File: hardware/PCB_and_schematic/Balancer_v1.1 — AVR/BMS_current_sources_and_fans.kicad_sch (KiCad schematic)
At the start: 90 parts, among them J11 HEATSING_TEMP1, J3 Conn_01x03, J4 HEATSING_TEMP1, J5 FAN1, J6 FAN2, J7 BATT_12V, Q10 TIP41C, Q11 TIP41C, Q12 BC817, Q13 BD238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

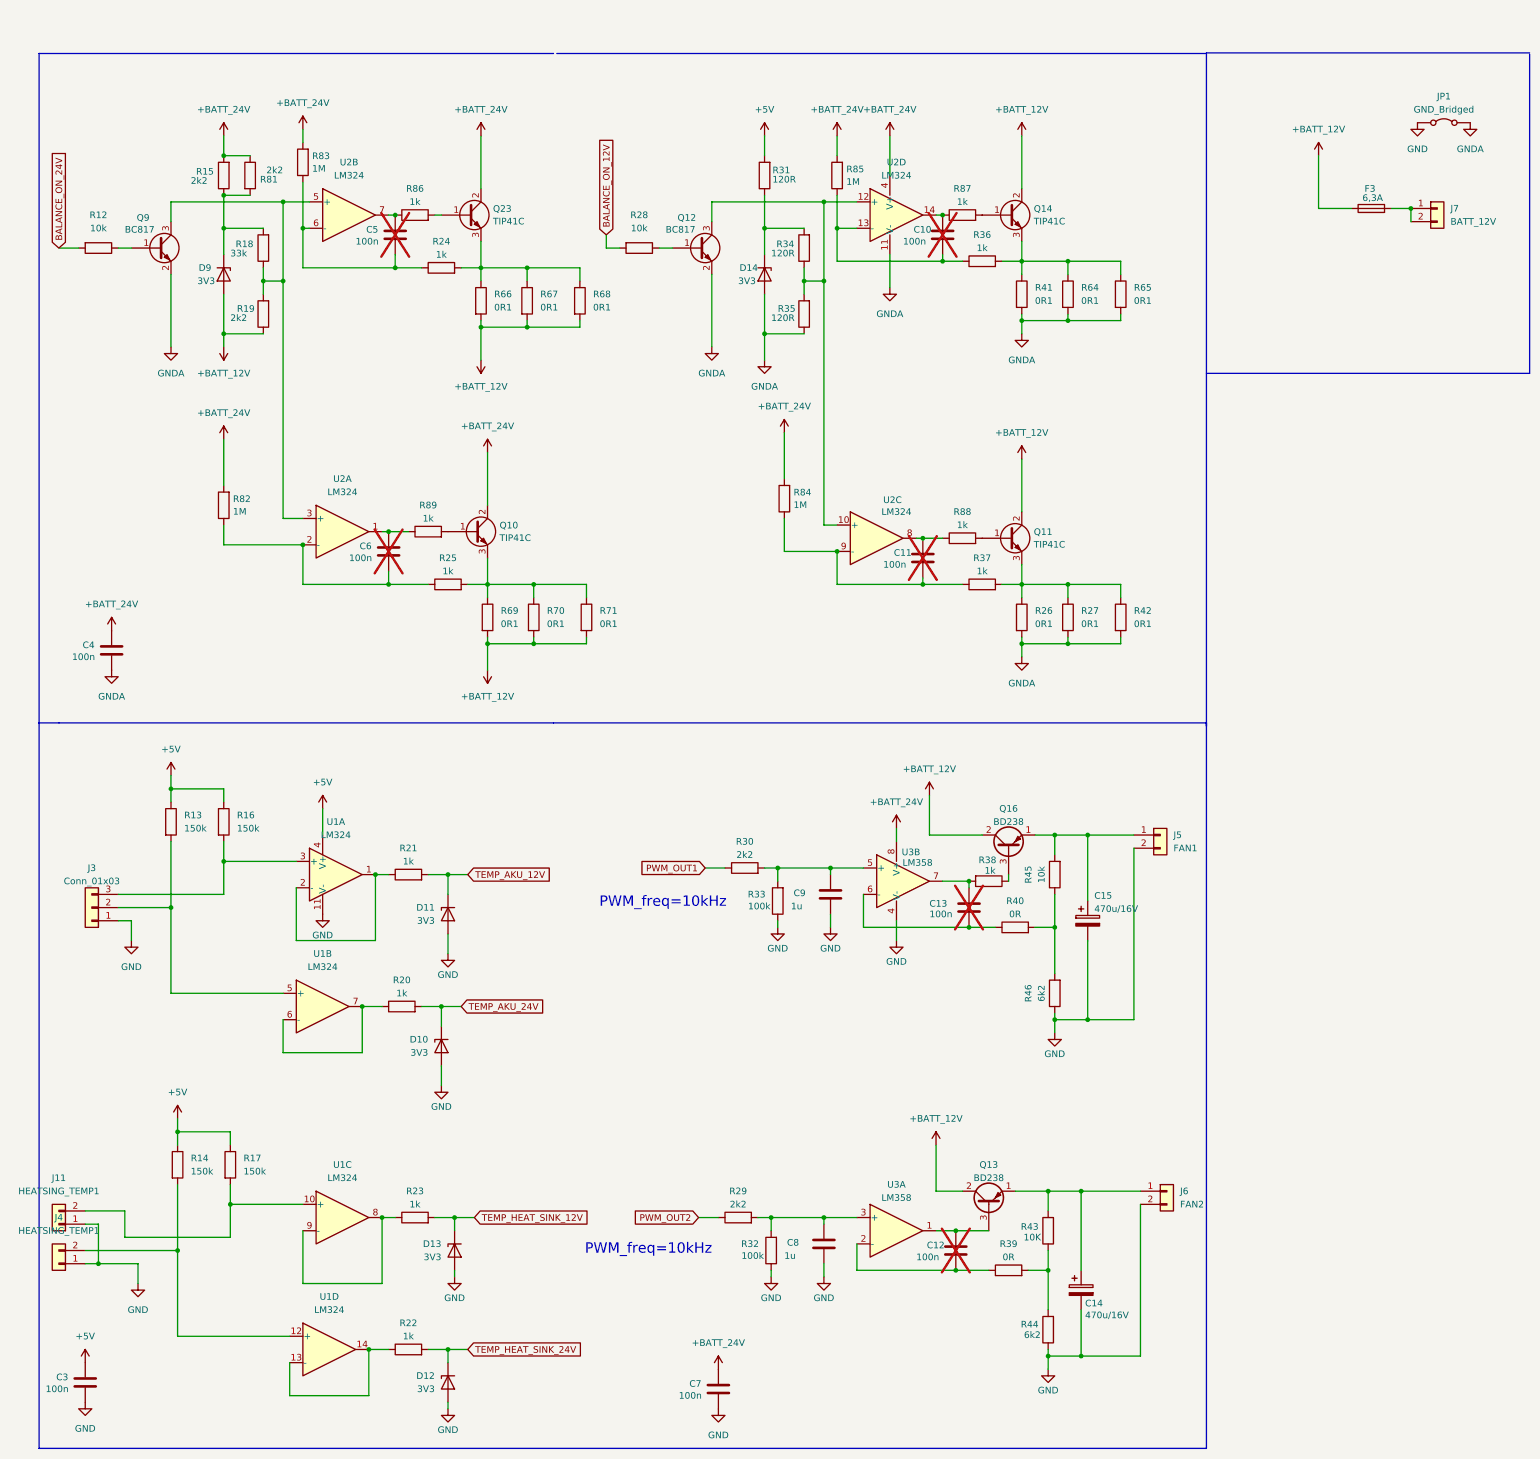
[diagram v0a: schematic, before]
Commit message: change uc on balancer
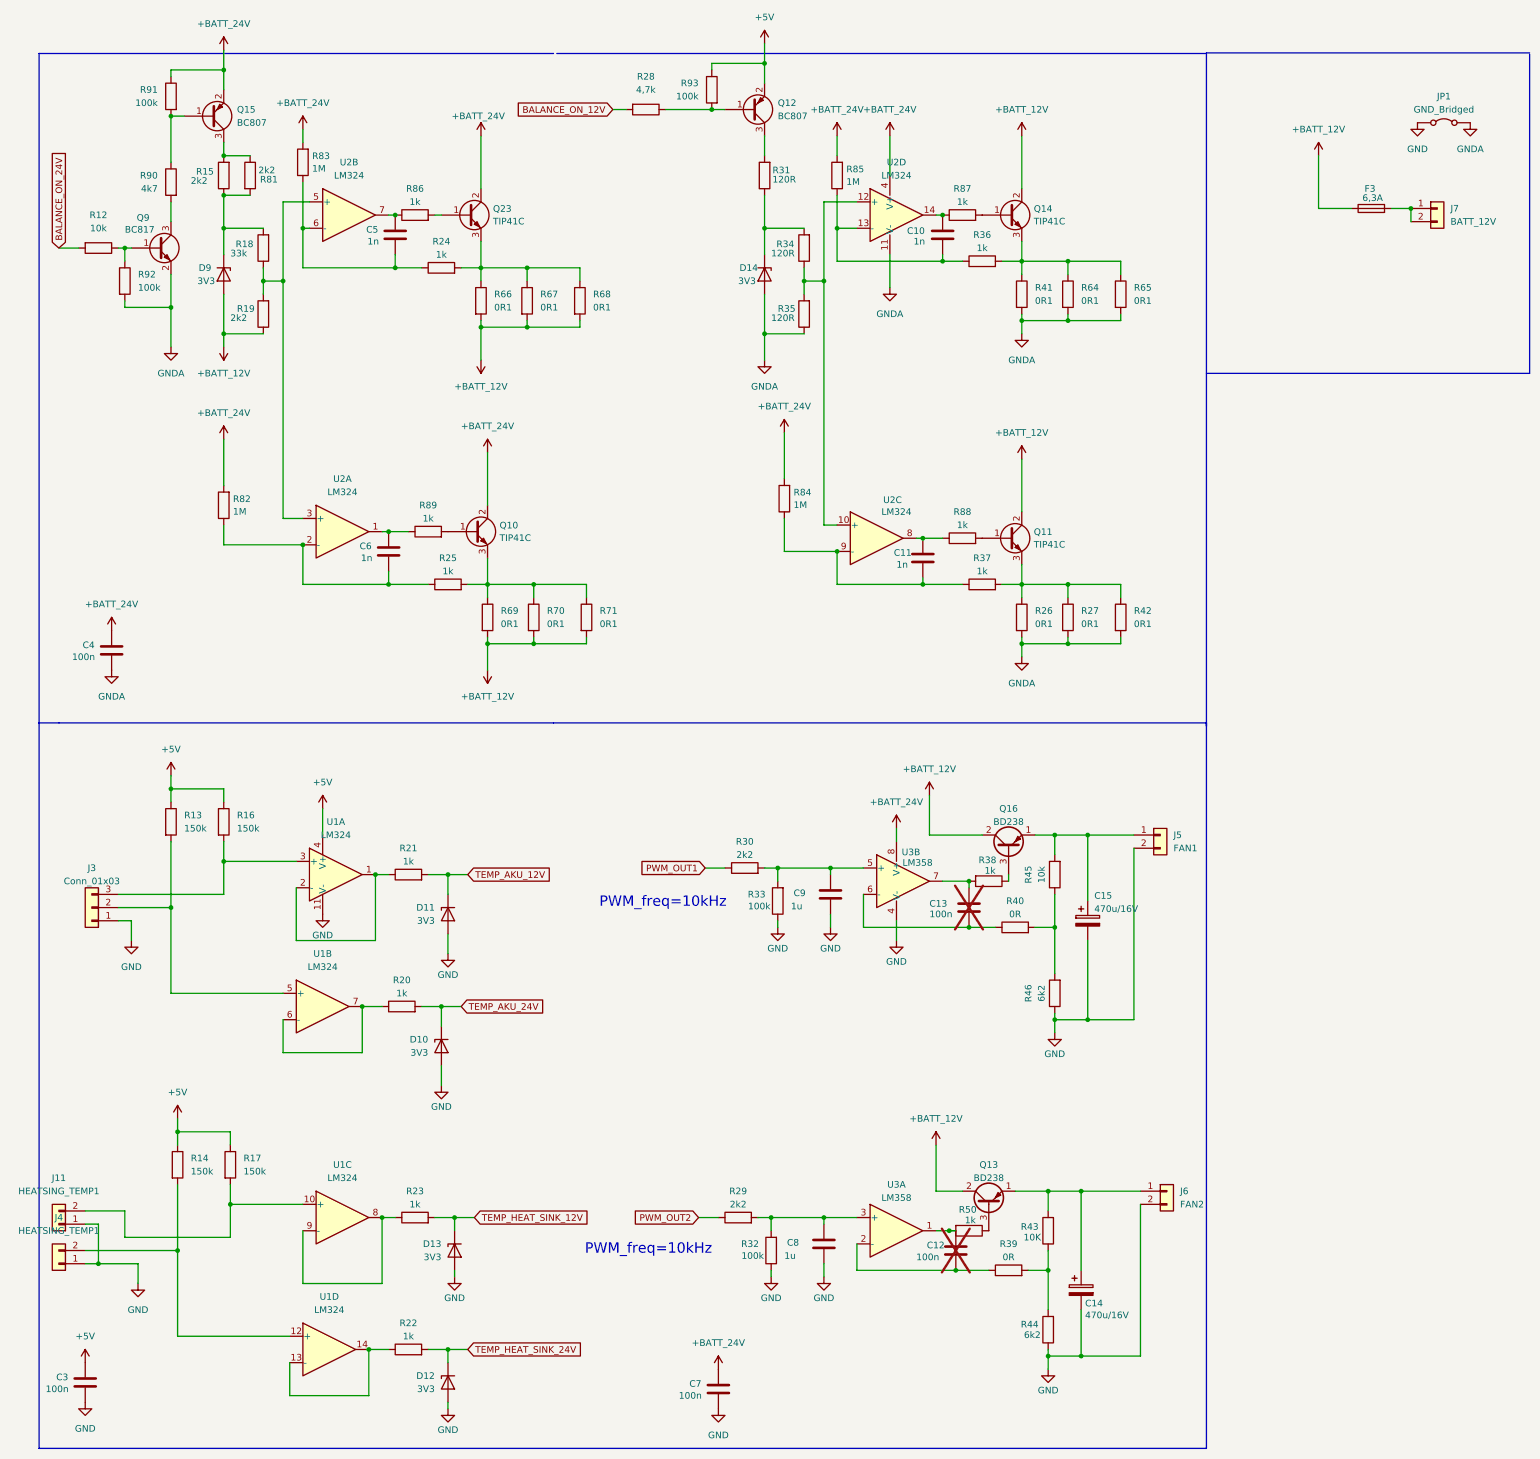
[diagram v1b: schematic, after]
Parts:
- removed Q12: BC817, Package_TO_SOT_SMD:SOT-23, symbol Transistor_BJT:BC817
- added Q12, Q15: BC807, Package_TO_SOT_SMD:SOT-23, symbol Transistor_BJT:BC807
- added R50: 1k, Resistor_SMD:R_0805_2012Metric_Pad1.20x1.40mm_HandSolder, symbol Device:R
- added R90: 4k7, Resistor_SMD:R_0805_2012Metric_Pad1.20x1.40mm_HandSolder, symbol Device:R
- added R91, R92, R93: 100k, Resistor_SMD:R_0805_2012Metric_Pad1.20x1.40mm_HandSolder, symbol Device:R
- C10, C11, C5, C6: value 100n -> 1n; now fitted
- R28: value 10k -> 4,7k
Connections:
- net +5V: now also Q12.2 (E), R93.1; no longer R31.2
- net +BATT_24V: now also Q15.2 (E), R91.1; no longer R15.2, R81.1
- net GNDA: now also R92.2
- net at Q9.1 (B), R12.1: now also R92.1
- net at R18.1, R19.2, U2.3 (+)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: no longer Q9.3 (C)
- net at C12.1, U3.1: now also R50.2; no longer Q13.3 (B)
- net at R28.1: now also Q12.1 (B), R93.2
- new net: Q13.3 (B), R50.1
- new net: Q15.3 (C), R15.2, R81.1
- new net: Q15.1 (B), R90.1, R91.2
- new net: Q9.3 (C), R90.2
- new net: Q12.3 (C), R31.2
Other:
- moved on the sheet: R28

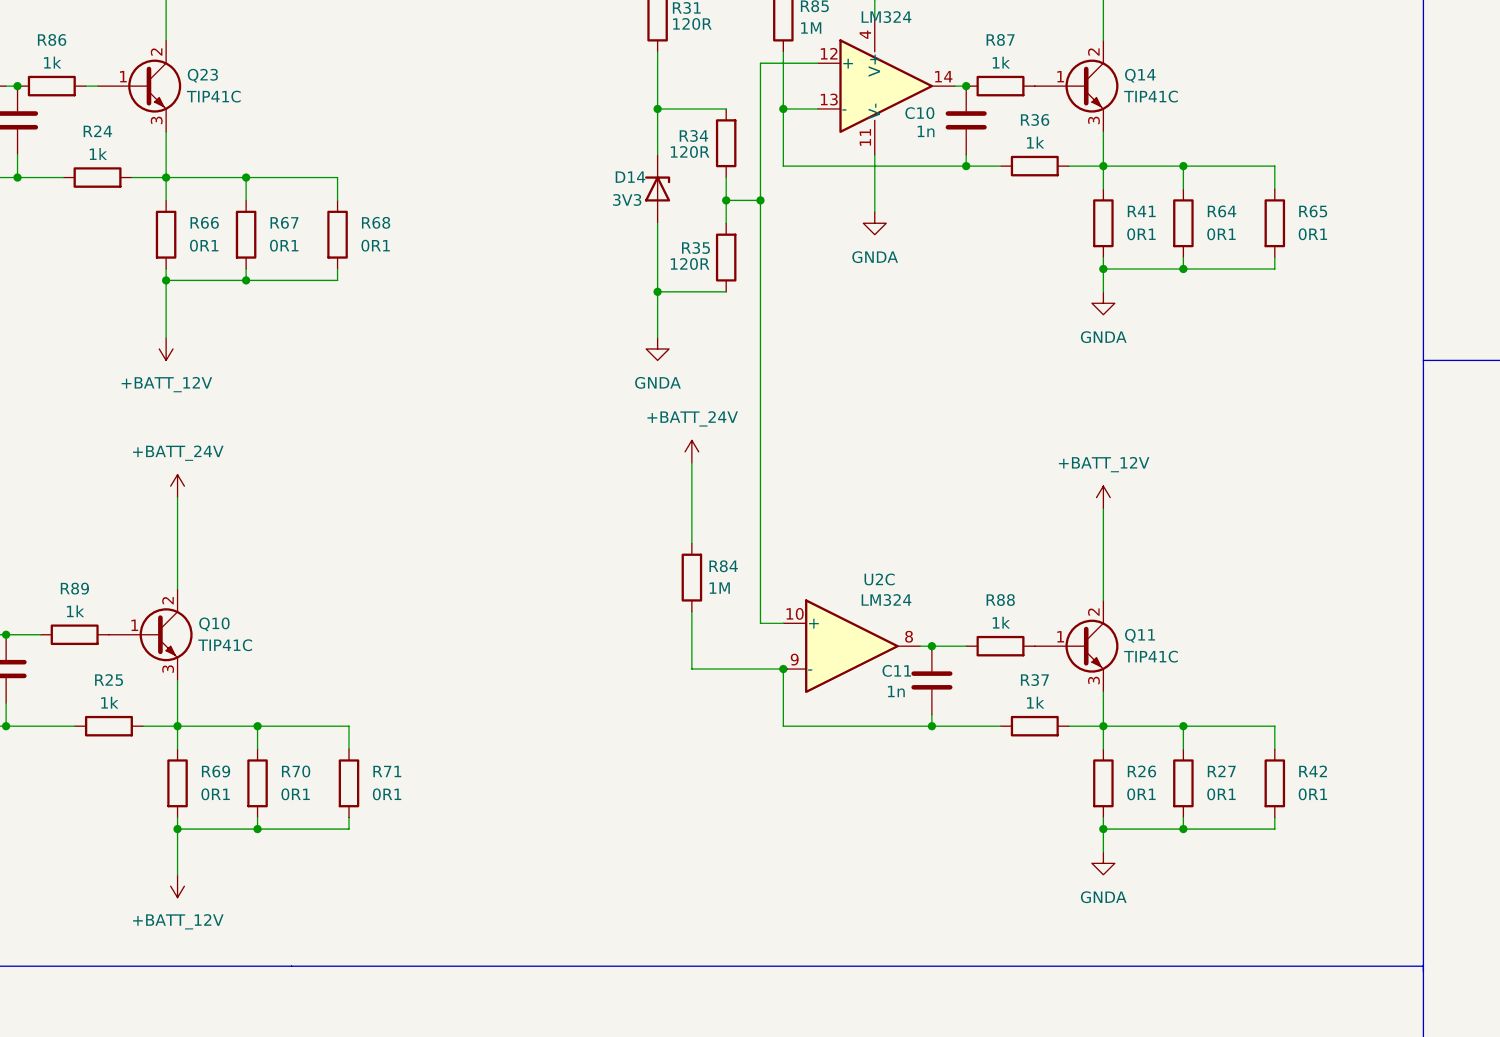
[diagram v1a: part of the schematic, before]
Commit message: change with balancer schematic, generate code for avr
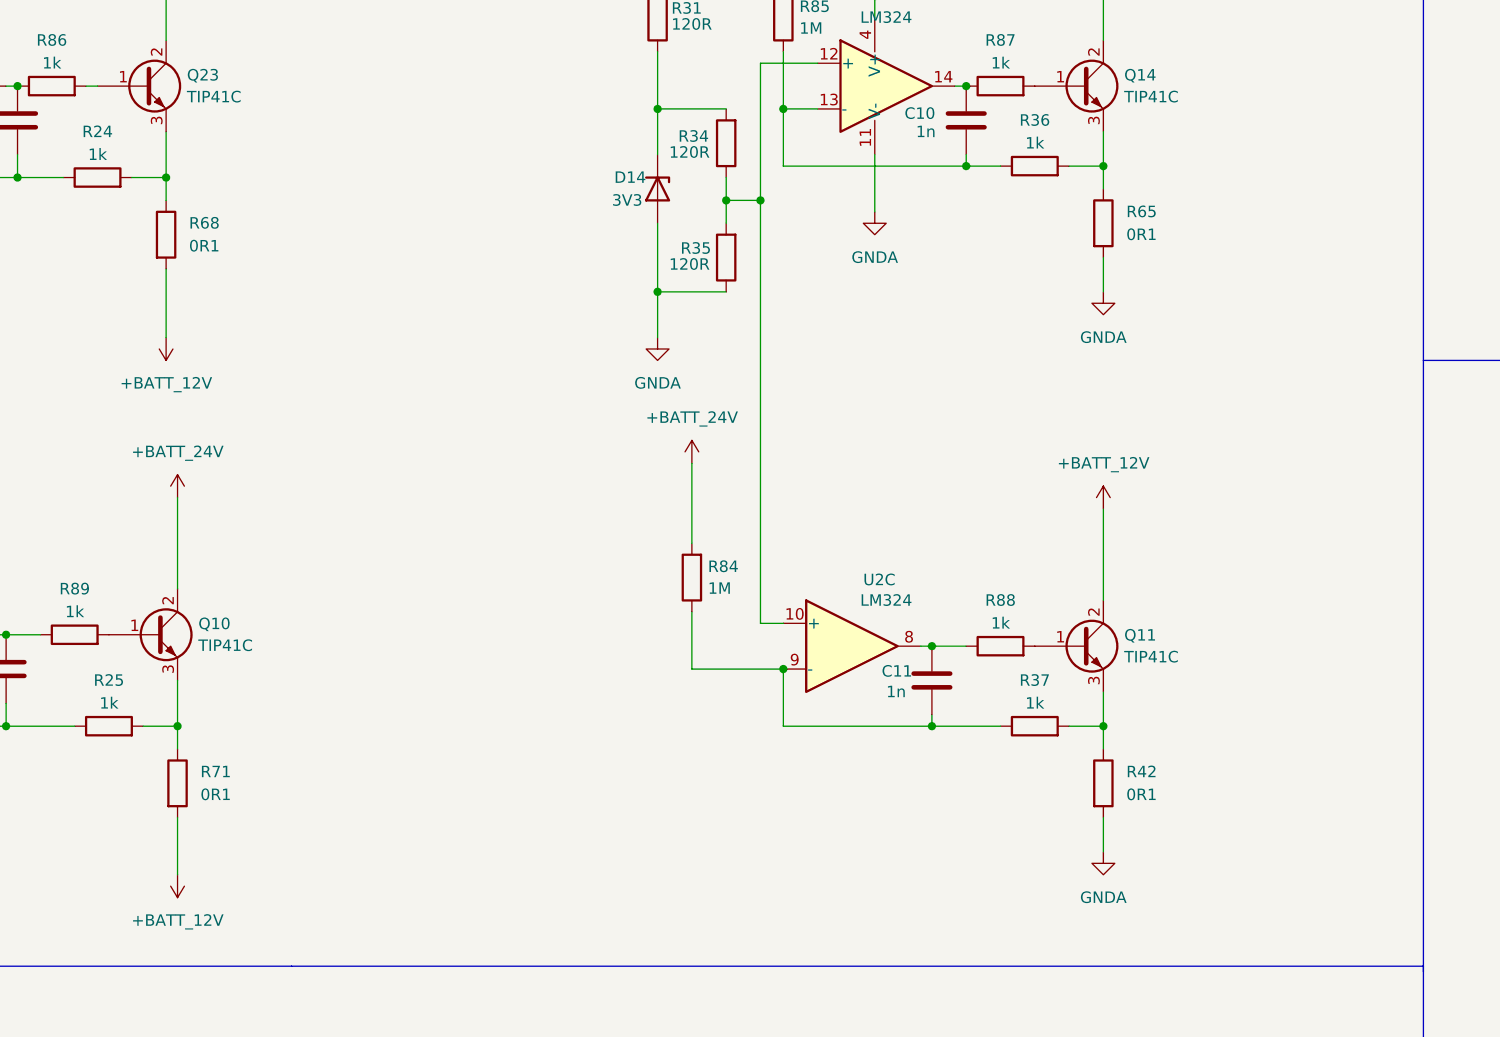
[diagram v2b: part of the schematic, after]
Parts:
- removed R26, R27, R41, R64, R66, R67, R69, R70: 0R1, Resistor_SMD:R_2512_6332Metric_Pad1.40x3.35mm_HandSolder, symbol Device:R
- R42, R65, R68, R71: footprint Resistor_THT:R_Axial_DIN0617_L17.0mm_D6.0mm_P7.62mm_Vertical -> My-Footprints:R_Axial_DIN0411_L9.9mm_D3.6mm_P12.70mm_Horizontal
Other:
- moved on the sheet: R42, R65, R68, R71

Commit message: values update
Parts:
- C10, C5, C6: value 1n -> 1n5
- R12: value 10k -> 1k
- R28: value 4,7k -> 1k
- R31: value 120R -> 220R
- R34: value 120R -> 33k
- R35: value 120R -> 2k2
- R90: value 4k7 -> 2k2
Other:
- note added: "Iz=7mA"
- note added: "V divider 33k 2k2 Vout=206mV I=93uA"
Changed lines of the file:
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@@
 		)
 	)
+	(text "V divider\n33k 2k2\nVout=206mV\nI=93uA"
+		(exclude_from_sim no)
+		(at 169.672 93.472 0)
+		(effects
+			(font
+				(size 1.27 1.27)
+			)
+			(justify left top)
+		)
+	)
 	(text "PWM_freq=10kHz"
 		(exclude_from_sim no)
@@
 		)
 	)
+	(text "Iz=7mA"
+		(exclude_from_sim no)
+		(at 181.864 76.962 0)
+		(effects
+			(font
+				(size 1.27 1.27)
+			)
+		)
+	)
 	(global_label "TEMP_AKU_24V"
 		(shape input)
@@
 			)
 		)
-		(property "Value" "10k"
+		(property "Value" "1k"
 			(at 59.69 86.36 90)
 			(effects
@@
 			)
 		)
-		(property "Value" "1n"
+		(property "Value" "1n5"
 			(at 111.506 88.9 0)
 			(effects
@@
 			)
 		)
-		(property "Value" "4,7k"
+		(property "Value" "1k"
 			(at 165.1 59.69 90)
 			(effects
@@
 			)
 		)
-		(property "Value" "120R"
+		(property "Value" "2k2"
 			(at 189.23 103.632 0)
 			(effects
@@
 			)
 		)
-		(property "Value" "1n"
+		(property "Value" "1n5"
 			(at 216.662 88.9 0)
 			(effects
@@
 			)
 		)
-		(property "Value" "120R"
+		(property "Value" "33k"
 			(at 189.23 91.186 0)
 			(effects
@@
 			)
 		)
-		(property "Value" "4k7"
+		(property "Value" "2k2"
 			(at 71.12 78.7399 0)
 			(effects
@@
 			)
 		)
-		(property "Value" "120R"
+		(property "Value" "220R"
 			(at 189.484 76.962 0)
 			(effects
@@
 			)
 		)
-		(property "Value" "1n"
+		(property "Value" "1n5"
 			(at 110.236 149.86 0)
 			(effects
